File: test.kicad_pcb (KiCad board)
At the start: 4 copper layers, 86.4 x 61 mm, 24 parts, among them J1 Conn_01x06_Female, J2 Conn_02x02_Top_Bottom, J3 Conn_02x03_Odd_Even, J4 Conn_01x02, J5 Conn_01x02, J6 Conn_02x02_Top_Bottom, J7 Conn_02x10_Counter_Clockwise, SW1 PTS647SK38SMTR2LFS, U1 PIC32MX340F512H-80I_MR

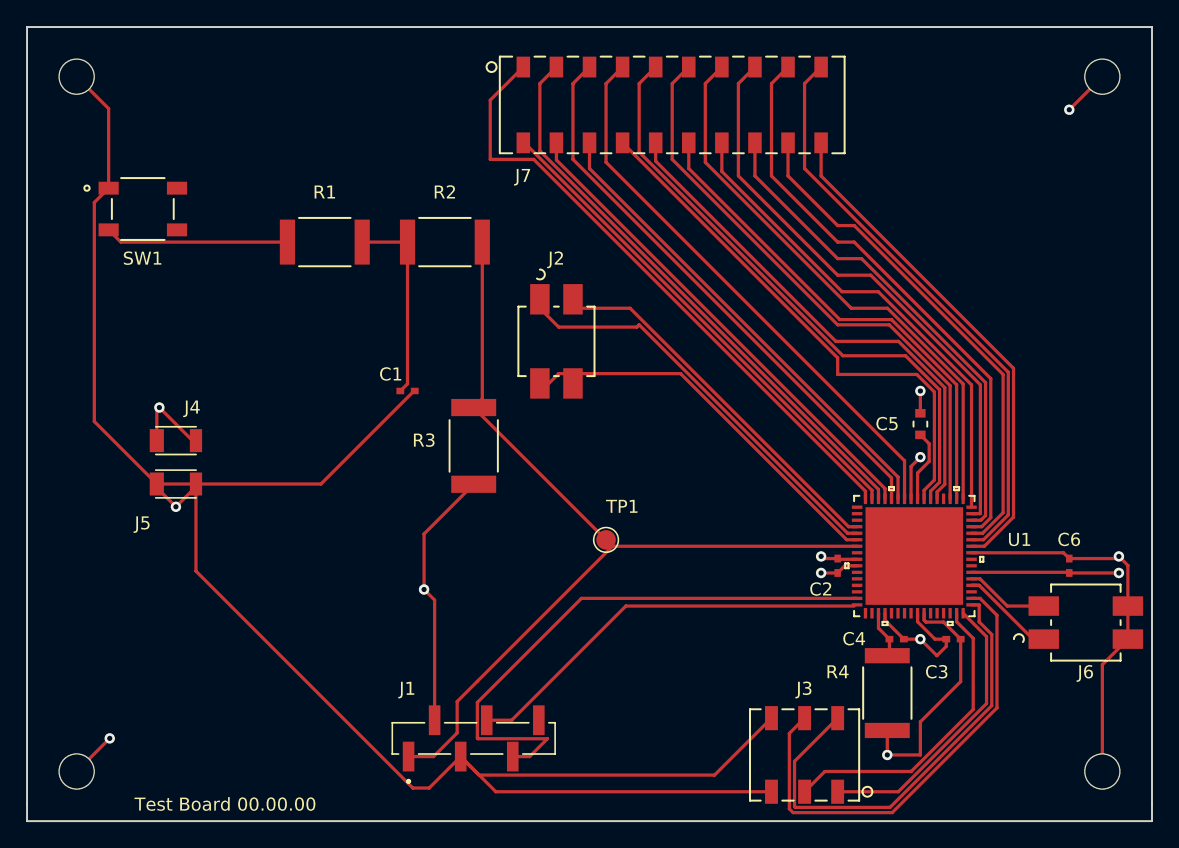
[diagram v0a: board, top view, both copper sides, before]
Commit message: - Reworked schematic with more recognizable symbols, more information, more adherent to FAQ, etc. - Shifted from 4 layer to 2 layer - Removed all micro/hidden vias - Standardized footprints for all resistors and capacitors - Shifted all headers from SMD to througholes - Added more information to silkscreen
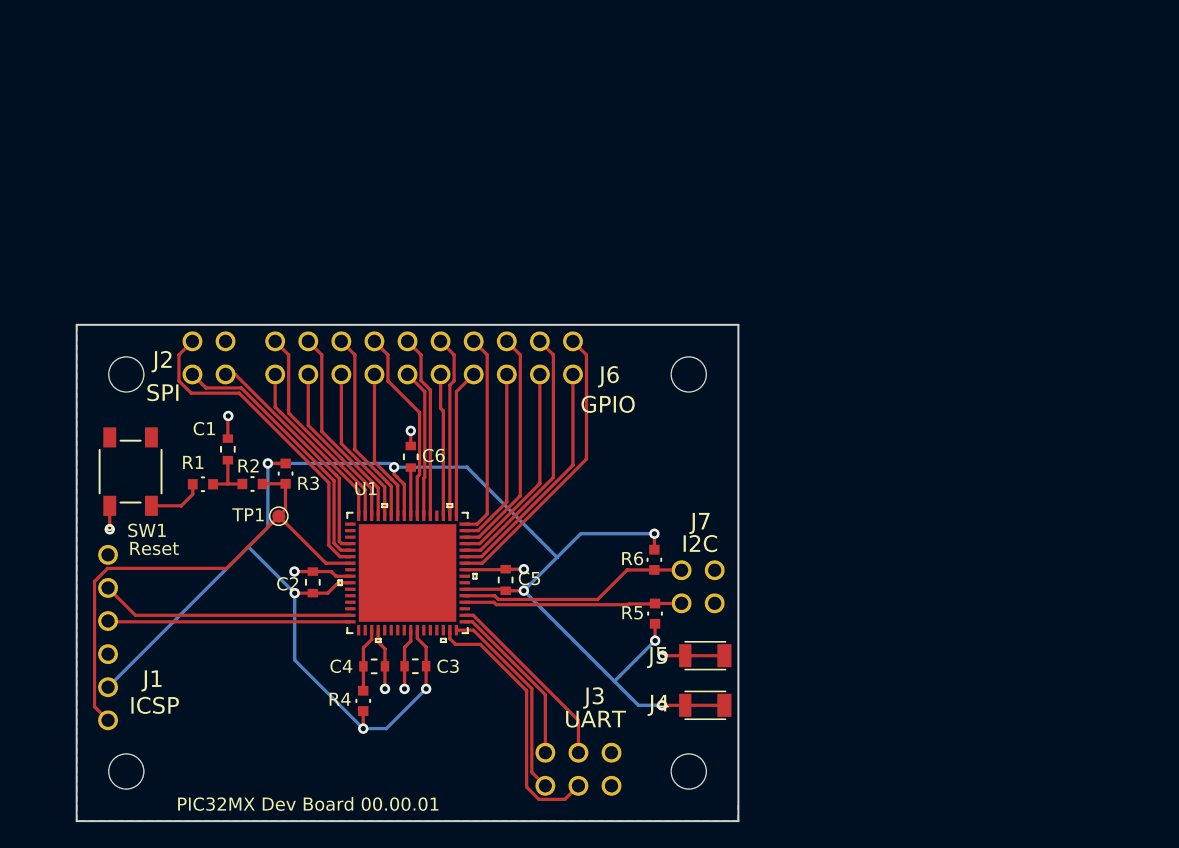
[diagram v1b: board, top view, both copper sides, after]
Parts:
- added R5: 4.7kΩ, mod:ERJ-3EKF10R0V, F.Cu at (150.3, 116.3)
- added R6: 4.7kΩ, mod:ERJ-3EKF10R0V, F.Cu at (150.2, 112.2)
- C1, C2, C3, C4: value CL05A104KA5NNNC -> 0.1uF; footprint mod:CL05A104KA5NNNC -> mod:CL10A106MQ8NNNC
- C5: value CL10A106MQ8NNNC -> 0.1uF
- C6: value CL05A104KA5NNNC -> 10uF; footprint mod:CL05A104KA5NNNC -> mod:CL10A106MQ8NNNC
- J1: value Conn_01x06_Female -> ICSP; footprint mod:SULLINS_NPPN061BFLD-RC -> mod:01x06
- J2: value Conn_02x02_Top_Bottom -> SPI; footprint mod:969973-2 -> mod:02x02
- J3: value Conn_02x03_Odd_Even -> UART; footprint mod:M20-7870346 -> mod:02x03
- J4: value Conn_01x02 -> 3.3v VDD
- J5: value Conn_01x02 -> VSS
- J6: value Conn_02x02_Top_Bottom -> GPIO; footprint mod:969973-2 -> mod:02x20
- J7: value Conn_02x10_Counter_Clockwise -> I2C; footprint mod:NPPC102KFMS-RC -> mod:02x02
- R1, R2: footprint mod:RMCF2512JT470R -> mod:ERJ-3EKF10R0V
- R3: footprint mod:RMCF2512FT10K0 -> mod:ERJ-3EKF10R0V
- R4: footprint mod:RMCF2512JT10R0 -> mod:ERJ-3EKF10R0V
- SW1: value PTS647SK38SMTR2LFS -> Reset
- TP1: footprint TestPoint:TestPoint_Pad_D1.5mm -> TestPoint:TestPoint_Pad_D1.0mm
- moved MK3 92.0 mm to (109.7, 128.4)
- moved MK1 71.1 mm to (152.9, 128.4)
- moved J6 65.9 mm to (121.1, 95.4), turned to 0 degrees
- moved C6 51.2 mm to (131.5, 104.3), turned to 90 degrees
- moved J4 45.4 mm to (154.1, 123.3), turned to 180 degrees
- moved MK4 44.0 mm to (152.9, 97.9)
- moved J5 42.7 mm to (154.1, 119.5), turned to 180 degrees
- moved C3 41.4 mm to (131.9, 120.3), turned to 180 degrees
- moved C2 40.3 mm to (124.0, 113.9), turned to 90 degrees
- moved R4 40.2 mm to (127.9, 123.0)
- moved C4 40.2 mm to (128.7, 120.3), turned to 180 degrees
- moved U1 38.9 mm to (131.3, 113.2)
- moved J7 35.9 mm to (154.9, 113.0), turned to 270 degrees
- moved C5 34.0 mm to (138.8, 113.7)
- moved MK2 30.7 mm to (109.7, 97.9)
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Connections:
- C1 pad 1: Net-(C1-Pad1) -> GNDREF
- C1 pad 2: GND -> Net-(C1-Pad2)
- C2 pad 1: GND -> +3V3
- C2 pad 2: +3V3 -> GNDREF
- C3 pad 1: GND -> +3V3
- C3 pad 2: +3V3 -> GNDREF
- C4 pad 1: Net-(C4-Pad1) -> GNDREF
- C4 pad 2: GND -> Net-(C4-Pad2)
- C5 pad 1: Net-(C5-Pad1) -> +3V3
- C5 pad 2: GND -> GNDREF
- C6 pad 1: GND -> Net-(C6-Pad1)
- C6 pad 2: +3V3 -> GNDREF
- J1 pad 3: GND -> GNDREF
- J3 pad 5: GND -> GNDREF
- J3 pad 6: GND -> GNDREF
- J5 pad 1: GND -> GNDREF
- J5 pad 2: GND -> GNDREF
- J6 pad 2: GND -> Net-(J6-Pad2)
- J6 pad 4: GND -> Net-(J6-Pad4)
- J7 pad 2: Net-(J7-Pad2) -> GNDREF
- J7 pad 4: Net-(J7-Pad4) -> GNDREF
- R1 pad 2: Net-(C1-Pad1) -> Net-(C1-Pad2)
- R2 pad 1: Net-(C1-Pad1) -> Net-(C1-Pad2)
- R4 pad 2: Net-(C4-Pad1) -> Net-(C4-Pad2)
- SW1 pad 1: GND -> GNDREF
- U1 pad 19: Net-(C4-Pad1) -> Net-(C4-Pad2)
- U1 pad 20: GND -> GNDREF
- U1 pad 25: GND -> GNDREF
- U1 pad 36: Net-(J6-Pad1) -> Net-(J7-Pad3)
- U1 pad 37: Net-(J6-Pad3) -> Net-(J7-Pad1)
- U1 pad 41: GND -> GNDREF
- U1 pad 42: Net-(J7-Pad20) -> Net-(J6-Pad20)
- U1 pad 43: Net-(J7-Pad19) -> Net-(J6-Pad19)
- U1 pad 44: Net-(J7-Pad18) -> Net-(J6-Pad18)
- U1 pad 45: Net-(J7-Pad17) -> Net-(J6-Pad17)
- U1 pad 46: Net-(J7-Pad16) -> Net-(J6-Pad16)
- U1 pad 47: Net-(J7-Pad15) -> Net-(J6-Pad15)
- U1 pad 48: Net-(J7-Pad14) -> Net-(J6-Pad14)
- U1 pad 49: Net-(J7-Pad13) -> Net-(J6-Pad13)
- U1 pad 50: Net-(J7-Pad12) -> Net-(J6-Pad12)
- U1 pad 51: Net-(J7-Pad11) -> Net-(J6-Pad11)
- U1 pad 53: Net-(J7-Pad10) -> Net-(J6-Pad10)
- U1 pad 54: Net-(J7-Pad9) -> Net-(J6-Pad9)
- U1 pad 55: Net-(J7-Pad8) -> Net-(J6-Pad8)
- U1 pad 56: Net-(C5-Pad1) -> Net-(C6-Pad1)
- U1 pad 58: Net-(J7-Pad7) -> Net-(J6-Pad7)
- U1 pad 59: Net-(J7-Pad6) -> Net-(J6-Pad6)
- U1 pad 60: Net-(J7-Pad5) -> Net-(J6-Pad5)
- U1 pad 61: Net-(J7-Pad4) -> Net-(J6-Pad4)
- U1 pad 62: Net-(J7-Pad3) -> Net-(J6-Pad3)
- U1 pad 63: Net-(J7-Pad2) -> Net-(J6-Pad2)
- U1 pad 64: Net-(J7-Pad1) -> Net-(J6-Pad1)
- U1 pad 9: GND -> GNDREF
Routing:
- net GND: track 200.0 -> 0.00 mm, vias 7 -> 0
- net +3V3: track 62.9 -> 129.7 mm, vias 6 -> 9
- net Net-(J7-Pad9): track 46.3 -> 0.00 mm
- net Net-(J7-Pad19): track 45.0 -> 0.00 mm
- net Net-(J7-Pad11): track 44.8 -> 0.00 mm
- net Net-(J7-Pad15): track 44.7 -> 0.00 mm
- net Net-(J7-Pad17): track 44.6 -> 0.00 mm
- net Net-(J7-Pad5): track 43.8 -> 0.00 mm
- net Net-(J7-Pad13): track 43.5 -> 0.00 mm
- net Net-(J7-Pad7): track 43.2 -> 0.00 mm
- net Net-(J7-Pad8): track 41.1 -> 0.00 mm
- net Net-(J7-Pad10): track 39.6 -> 0.00 mm
- net Net-(J7-Pad18): track 39.1 -> 0.00 mm
- net Net-(J7-Pad20): track 39.0 -> 0.00 mm
- net Net-(J7-Pad2): track 38.5 -> 0.00 mm
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- added copper zone on B.Cu, net GNDREF
- removed copper zone on 3.3V_Power, net +3V3
- removed copper zone on GND, net GND
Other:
- board size 86.4 x 61 mm -> 50.8 x 38.1 mm
- copper layers 4 -> 2
- board text added: "PIC32MX Dev Board 00.00.01"
- board text removed: "Test Board 00.00.00"

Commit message: - Changed board size to 1" by 2" - added 40mil exclusion zone from board edges - changed default trace to 8 mil - changed exclusion to 8 mil - changed power traces to 12 mil - added more descriptive silkscreen
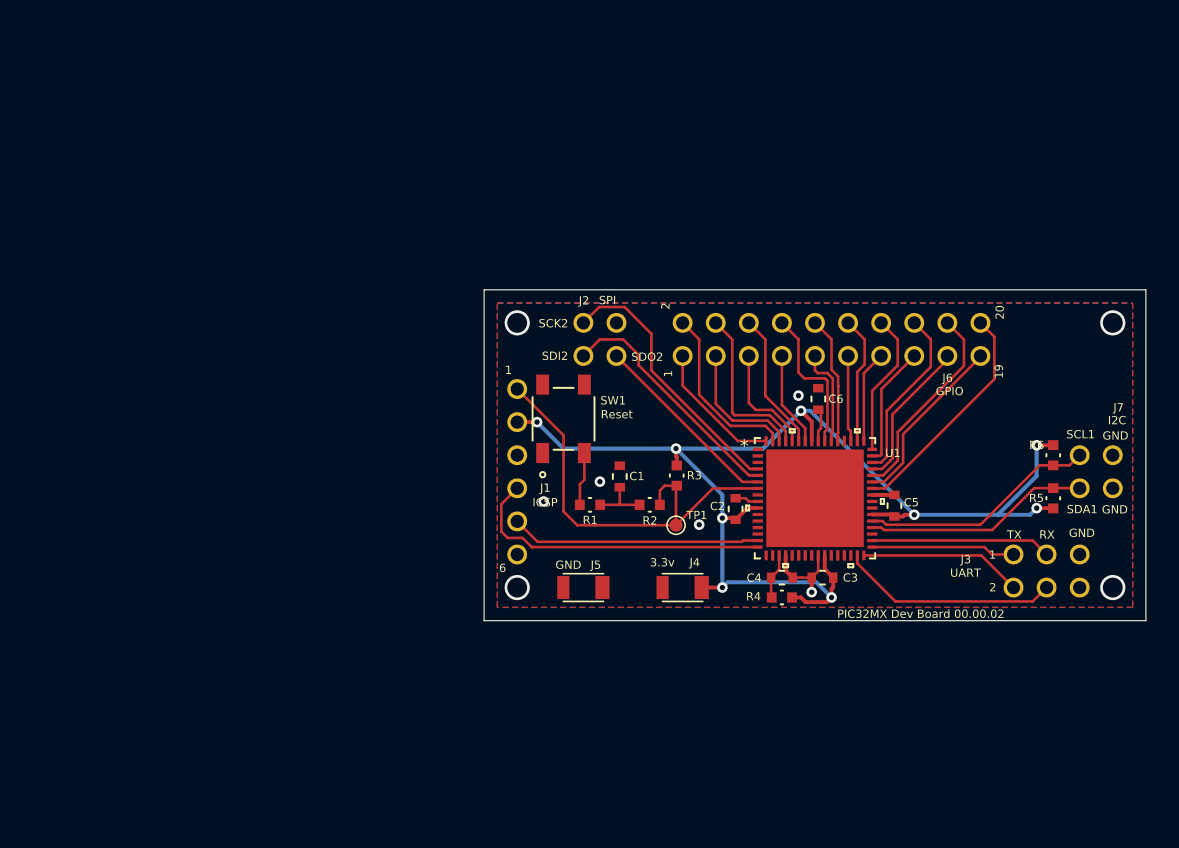
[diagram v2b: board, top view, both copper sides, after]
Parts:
- removed MK1, MK2, MK3, MK4: Mounting_Hole_PAD, MountingHole:MountingHole_2.7mm
- moved J1 40.4 mm to (139.7, 99.1), turned to 270 degrees
- moved J3 39.0 mm to (177.8, 111.8)
- moved SW1 33.5 mm to (143.3, 101.3)
- moved R4 33.1 mm to (160.0, 115.1), turned to 180 degrees
- moved C2 32.9 mm to (156.5, 108.3)
- moved C4 32.0 mm to (160.0, 113.5)
- moved C3 32.0 mm to (163.1, 113.5)
- moved R5 31.8 mm to (180.8, 107.4)
- moved U1 31.8 mm to (162.6, 107.4)
- moved R6 31.7 mm to (180.8, 104.1)
- moved C6 31.6 mm to (162.8, 99.8)
- moved J6 31.3 mm to (152.4, 94.0)
- moved R2 30.5 mm to (149.9, 108.0)
- moved TP1 30.5 mm to (151.9, 109.5)
- moved C5 30.4 mm to (168.7, 108.0)
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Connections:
- J4 pad 2: +3V3 -> Net-(J4-Pad2)
- J5 pad 2: GNDREF -> Net-(J5-Pad2)
- J7 pad 2: GNDREF -> Net-(J7-Pad2)
- J7 pad 3: Net-(J7-Pad3) -> GNDREF
- R5 pad 1: Net-(J7-Pad3) -> Net-(J7-Pad1)
- R6 pad 1: Net-(J7-Pad1) -> Net-(J7-Pad2)
- U1 pad 36: Net-(J7-Pad3) -> Net-(J7-Pad1)
- U1 pad 37: Net-(J7-Pad1) -> Net-(J7-Pad2)
- U1 pad 4: Net-(J2-Pad3) -> Net-(J2-Pad2)
- U1 pad 6: Net-(J2-Pad2) -> Net-(J2-Pad3)
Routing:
- net +3V3: track 129.7 -> 94.9 mm
- net Net-(J7-Pad2): track 0.00 -> 18.3 mm
- net GNDREF: track 27.9 -> 9.93 mm, vias 8 -> 9
- net Net-(J7-Pad3): track 16.8 -> 0.00 mm
- net Net-(J1-Pad1): track 38.8 -> 33.0 mm
- net Net-(J1-Pad4): track 18.6 -> 24.0 mm
- net Net-(J6-Pad14): track 15.7 -> 11.0 mm
- net Net-(J6-Pad15): track 13.9 -> 9.36 mm
- net Net-(J6-Pad17): track 16.1 -> 11.5 mm
- net Net-(J6-Pad19): track 18.2 -> 13.6 mm
- net Net-(J6-Pad20): track 22.1 -> 17.6 mm
- net Net-(J6-Pad16): track 17.9 -> 13.5 mm
- net Net-(J6-Pad18): track 20.0 -> 15.6 mm
- net Net-(J2-Pad2): track 25.0 -> 20.7 mm
- net Net-(J6-Pad13): track 11.4 -> 7.08 mm
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- added copper zone on F.Cu, net GNDREF
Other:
- board size 50.8 x 38.1 mm -> 50.8 x 25.4 mm
- net class Default: clearance 0.15 -> 0.2032; trace_width 0.25 -> 0.2032; via_dia 0.8 -> 0.8128; via_drill 0.4 -> 0.4064
- rule trace_clearance: 0.15 -> 0.2032
- rule trace_min: 0.2 -> 0.2032
- rule via_min_size: 0.4 -> 0.4064
- board text added: "1"
- board text added: "19"
- board text added: "2"
- board text added: "20"
- board text added: "3.3v"
- board text added: "6"
- board text added: "GND"
- board text added: "PIC32MX Dev Board 00.00.02"
- board text added: "RX"
- board text added: "SCK2"
- board text added: "SCL1"
- board text added: "SDA1"
- board text added: "SDI2"
- board text added: "SDO2"
- board text added: "TX"
- board text removed: "PIC32MX Dev Board 00.00.01"

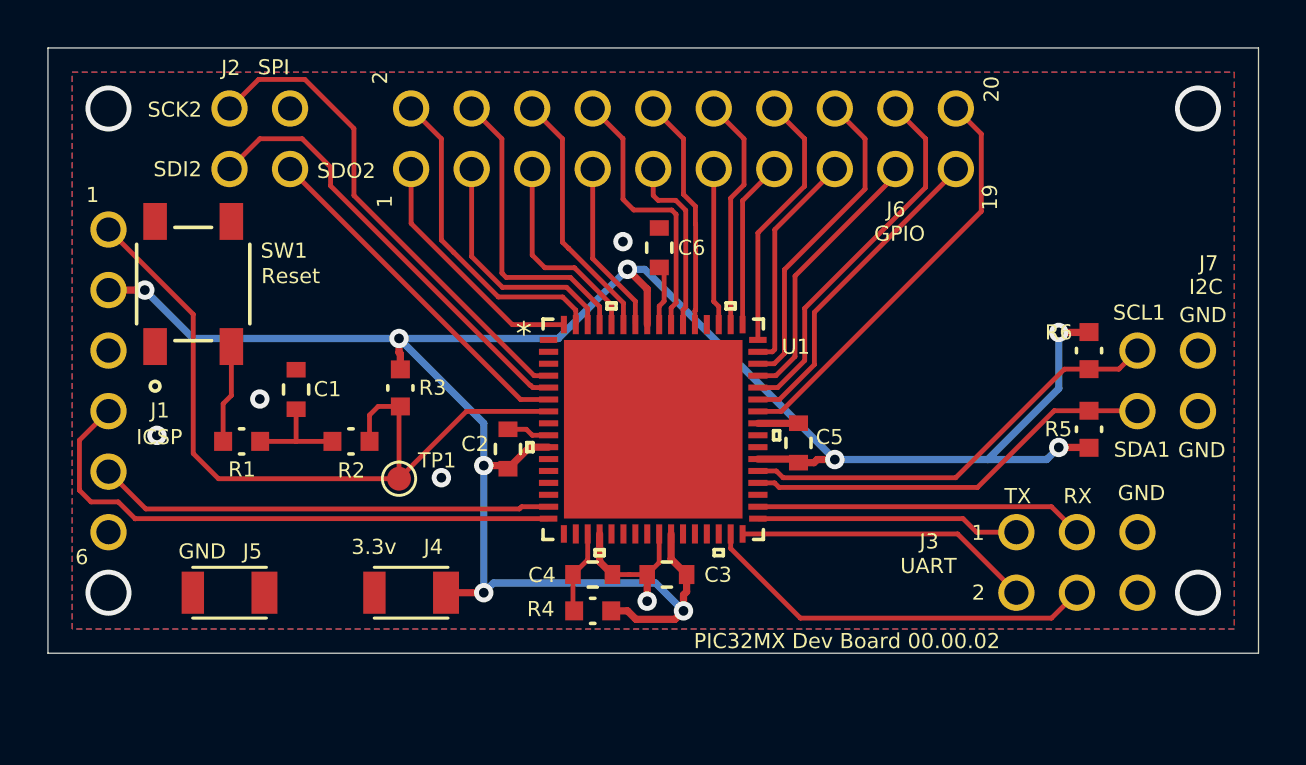
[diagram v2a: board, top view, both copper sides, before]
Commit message: - Added 4 User LEDs - Added 1 Power LED - Added 5 68ohm resistors to complement above LEDs - Reshaped board to 1.8"-1.1" - Added pin 52 to / Removed pin 42 from GPIO header (traded an INT for an extra OC/CN) - Reverted changed to corner pads for PIC back to original Microchip pad, just changed local clearances for those 8 pads - Added more silkscreen/rotated all existing silkscreen to face one way
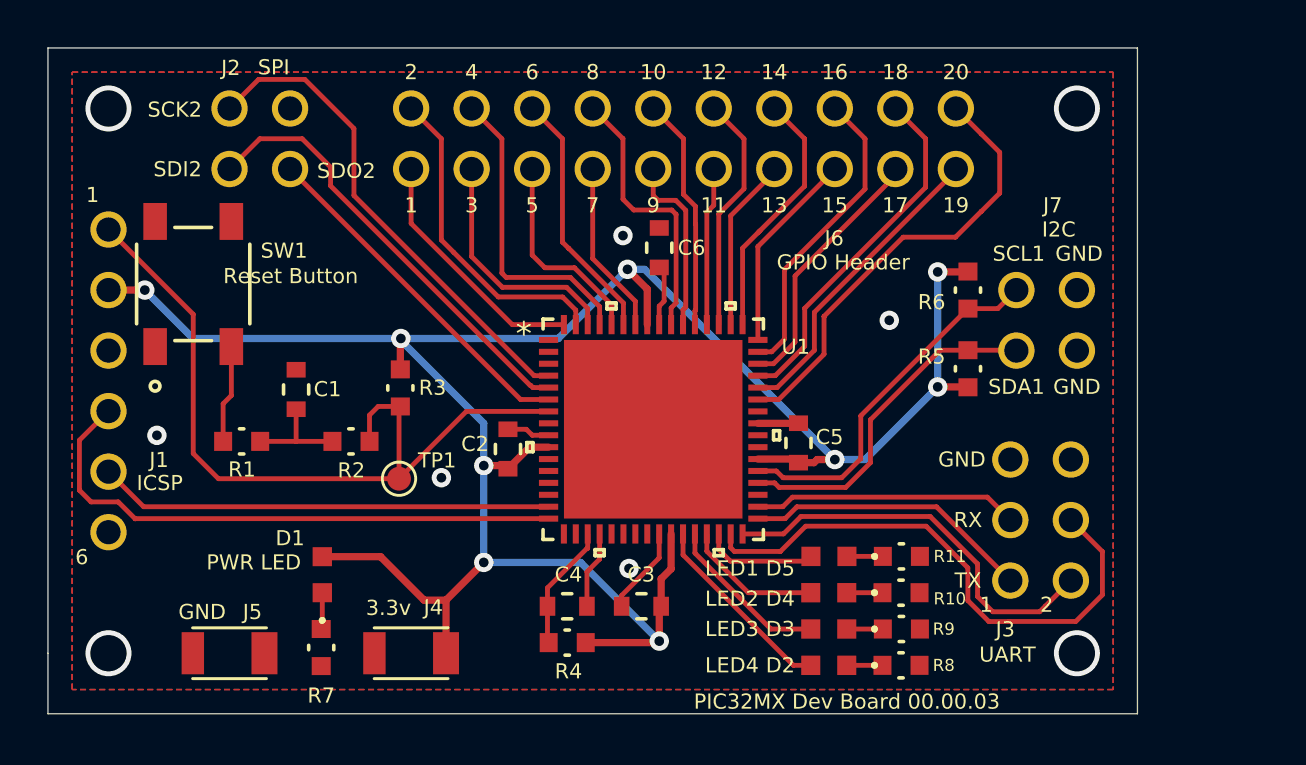
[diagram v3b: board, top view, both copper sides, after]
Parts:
- added D1: PWR LED, mod:LTST-C191KGKT, F.Cu at (148.7, 113.5)
- added D2: LED4, mod:LTST-C191KGKT, F.Cu at (169.9, 117.3)
- added D3: LED3, mod:LTST-C191KGKT, F.Cu at (169.9, 115.8)
- added D4: LED2, mod:LTST-C191KGKT, F.Cu at (169.9, 114.3)
- added D5: LED1, mod:LTST-C191KGKT, F.Cu at (169.9, 112.8)
- added R10: 68Ω, mod:ERJ-3EKF10R0V, F.Cu at (173.0, 114.3)
- added R11: 68Ω, mod:ERJ-3EKF10R0V, F.Cu at (173.0, 112.8)
- added R7: 68Ω, mod:ERJ-3EKF10R0V, F.Cu at (148.6, 116.6)
- added R8: 68Ω, mod:ERJ-3EKF10R0V, F.Cu at (173.0, 117.3)
- added R9: 68Ω, mod:ERJ-3EKF10R0V, F.Cu at (173.0, 115.8)
- J6: value GPIO -> GPIO Header
- SW1: value Reset -> Reset Button
- moved R6 5.68 mm to (175.8, 101.6)
- moved R5 5.68 mm to (175.8, 104.9)
- moved J7 5.68 mm to (177.8, 101.6)
- moved J4 2.54 mm to (152.4, 116.8)
- moved J5 2.54 mm to (144.8, 116.8)
- moved J3 2.05 mm to (177.5, 113.8), turned to 90 degrees
- moved C3 1.71 mm to (162.1, 114.9)
- moved C4 1.71 mm to (158.9, 114.9)
- moved R4 1.71 mm to (158.9, 116.4)
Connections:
- U1 pad 42: Net-(J6-Pad20) -> Net-(U1-Pad42)
- U1 pad 43: Net-(J6-Pad19) -> Net-(J6-Pad20)
- U1 pad 44: Net-(J6-Pad18) -> Net-(J6-Pad19)
- U1 pad 45: Net-(J6-Pad17) -> Net-(J6-Pad18)
- U1 pad 46: Net-(J6-Pad16) -> Net-(J6-Pad17)
- U1 pad 47: Net-(J6-Pad15) -> Net-(J6-Pad16)
- U1 pad 48: Net-(J6-Pad14) -> Net-(J6-Pad15)
- U1 pad 49: Net-(J6-Pad13) -> Net-(J6-Pad14)
- U1 pad 50: Net-(J6-Pad12) -> Net-(J6-Pad13)
- U1 pad 51: Net-(J6-Pad11) -> Net-(J6-Pad12)
- U1 pad 52: Net-(U1-Pad52) -> Net-(J6-Pad11)
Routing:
- net Net-(D2-Pad2): track 0.00 -> 8.16 mm
- net Net-(D3-Pad2): track 0.00 -> 6.98 mm
- net Net-(J3-Pad3): track 16.8 -> 23.3 mm
- net Net-(D4-Pad2): track 0.00 -> 5.81 mm
- net Net-(D5-Pad2): track 0.00 -> 4.81 mm
- net Net-(J3-Pad1): track 12.5 -> 17.1 mm
- net Net-(J7-Pad1): track 17.3 -> 14.4 mm
- net Net-(J7-Pad2): track 18.3 -> 15.3 mm
- net Net-(J3-Pad4): track 13.8 -> 11.2 mm
- net +3V3: track 94.9 -> 97.3 mm
- net Net-(C4-Pad2): track 3.50 -> 5.30 mm
- net Net-(D3-Pad1): track 0.00 -> 1.51 mm
- net Net-(D5-Pad1): track 0.00 -> 1.51 mm
- net Net-(D4-Pad1): track 0.00 -> 1.50 mm
- net Net-(D2-Pad1): track 0.00 -> 1.50 mm
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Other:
- board size 50.8 x 25.4 mm -> 45.7 x 27.9 mm
- board text added: "10"
- board text added: "11"
- board text added: "12"
- board text added: "13"
- board text added: "14"
- board text added: "15"
- board text added: "16"
- board text added: "17"
- board text added: "18"
- board text added: "3"
- board text added: "4"
- board text added: "5"
- board text added: "7"
- board text added: "8"
- board text added: "9"
- board text added: "PIC32MX Dev Board 00.00.03"
- board text removed: "PIC32MX Dev Board 00.00.02"
